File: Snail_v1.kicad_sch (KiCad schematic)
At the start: 29 parts, among them J1 PWM_Connector, J5 Conn_ARM_SWD_TagConnect_TC203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, U1 STM32G431K6Tx

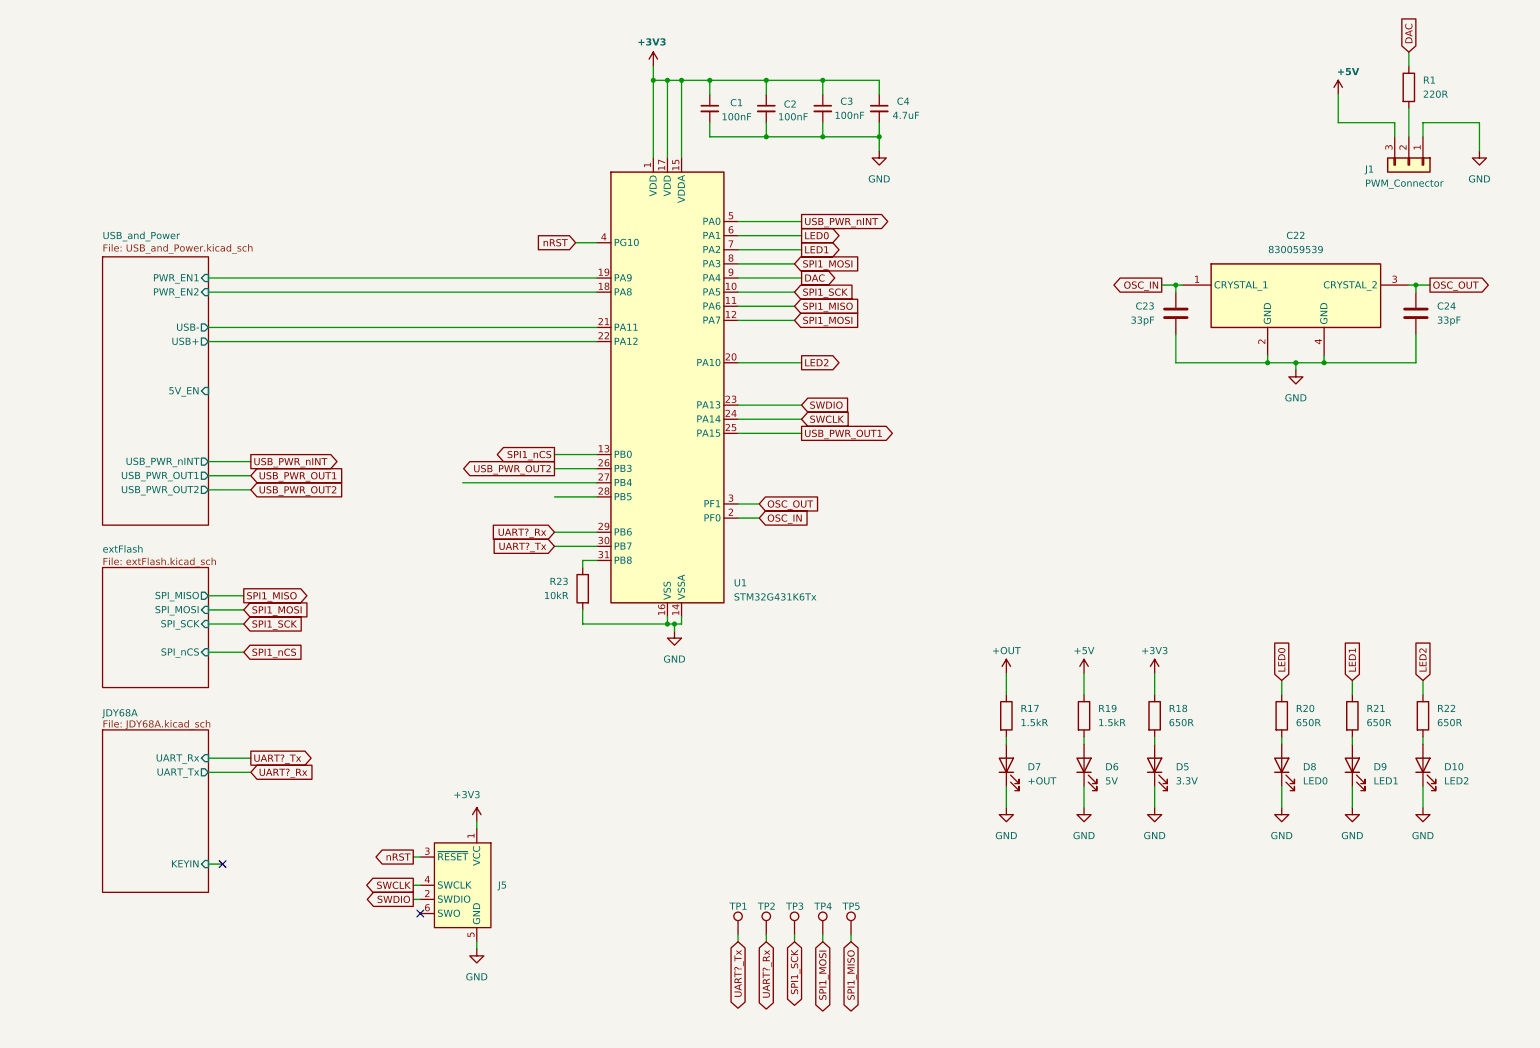
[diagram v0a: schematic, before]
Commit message: Did Silkscreen + added images of PCBA
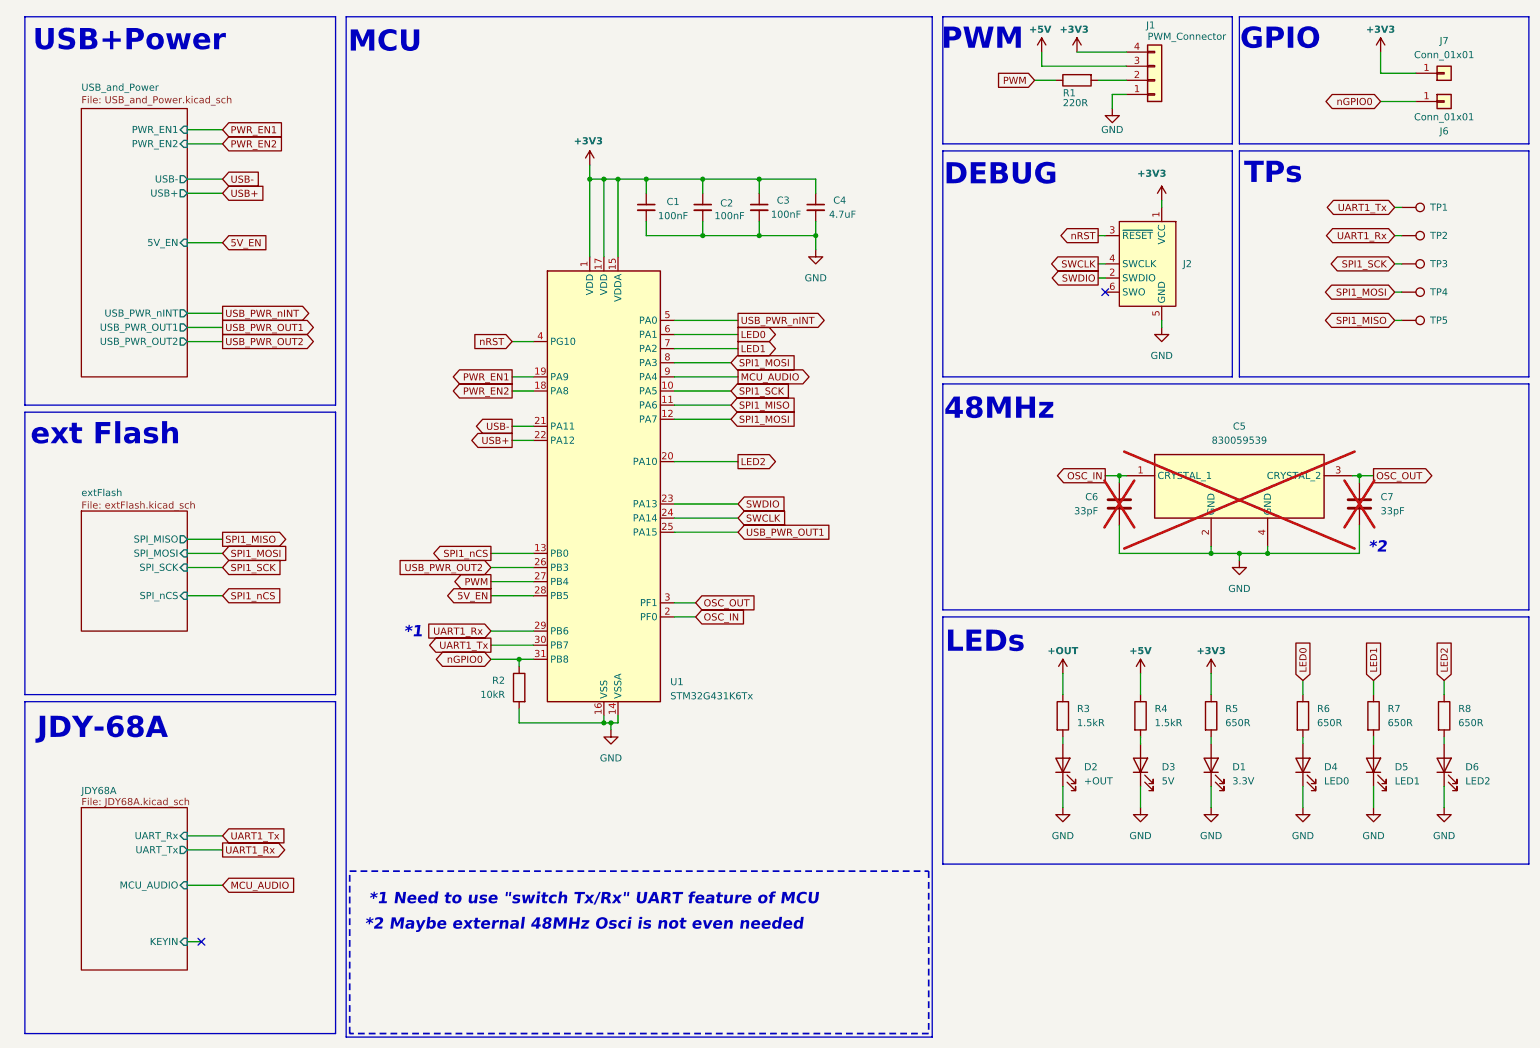
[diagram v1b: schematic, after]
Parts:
- removed J1: PWM_Connector, Connector_PinHeader_2.54mm:PinHeader_1x03_P2.54mm_Vertical, symbol Connector_Generic:Conn_01x03
- added J1: PWM_Connector, Connector_PinHeader_2.54mm:PinHeader_1x04_P2.54mm_Vertical, symbol Connector_Generic:Conn_01x04
- added J6, J7: Conn_01x01, Connector_Wire:SolderWirePad_1x01_SMD_1.5x3mm, symbol Connector_Generic:Conn_01x01
- C5: renamed from C22; now not fitted
- C6: renamed from C23; now not fitted
- C7: renamed from C24; now not fitted
- renumbered D5 to D1, D7 to D2, D6 to D3, D8 to D4, D9 to D5, D10 to D6, J5 to J2, R23 to R2, R17 to R3, R19 to R4, R18 to R5, R20 to R6, R21 to R7, R22 to R8
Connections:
- net +3V3: now also J1.4 (Pin_4), J7.1 (Pin_1)
- net +5V: now also J1.3 (Pin_3)
- net GND: now also J1.1 (Pin_1)
- net at R1.2: now also J1.2 (Pin_2)
- net PWM: now reaches U1.27 (PB4)
- net PWM: now also R1.1
- net 5V_EN: now reaches U1.28 (PB5)
- net nGPIO0: now reaches R2.1, U1.31 (PB8)
- net nGPIO0: now also J6.1 (Pin_1)
- net DAC renamed MCU_AUDIO
- net MCU_AUDIO: no longer R1.1
- net UART?_Rx renamed UART1_Rx
- net UART?_Tx renamed UART1_Tx
- net USB_and_Power/PWR_EN1 renamed PWR_EN1
- net USB_and_Power/PWR_EN2 renamed PWR_EN2
- net USB_and_Power/USB+ renamed USB+
- net USB_and_Power/USB- renamed USB-
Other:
- sheet JDY68A ports: added MCU_AUDIO; removed none
- note added: "*1"
- note added: "*1 Need to use "switch Tx/Rx" UART feature of MCU"
- note added: "*2"
- note added: "*2 Maybe external 48MHz Osci is not even needed"
- note added: "48MHz"
- note added: "DEBUG"
- note added: "GPIO"
- note added: "JDY-68A"
- note added: "LEDs"
- note added: "MCU"
- note added: "PWM"
- note added: "TPs"
- note added: "USB+Power"
- note added: "ext Flash"
- moved on the sheet: C1, C2, C3, C4, D1, D2, D3, D4, D5, D6, J2, R1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

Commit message: Added missing AMP_nSD connection to MCU via 5V_EN
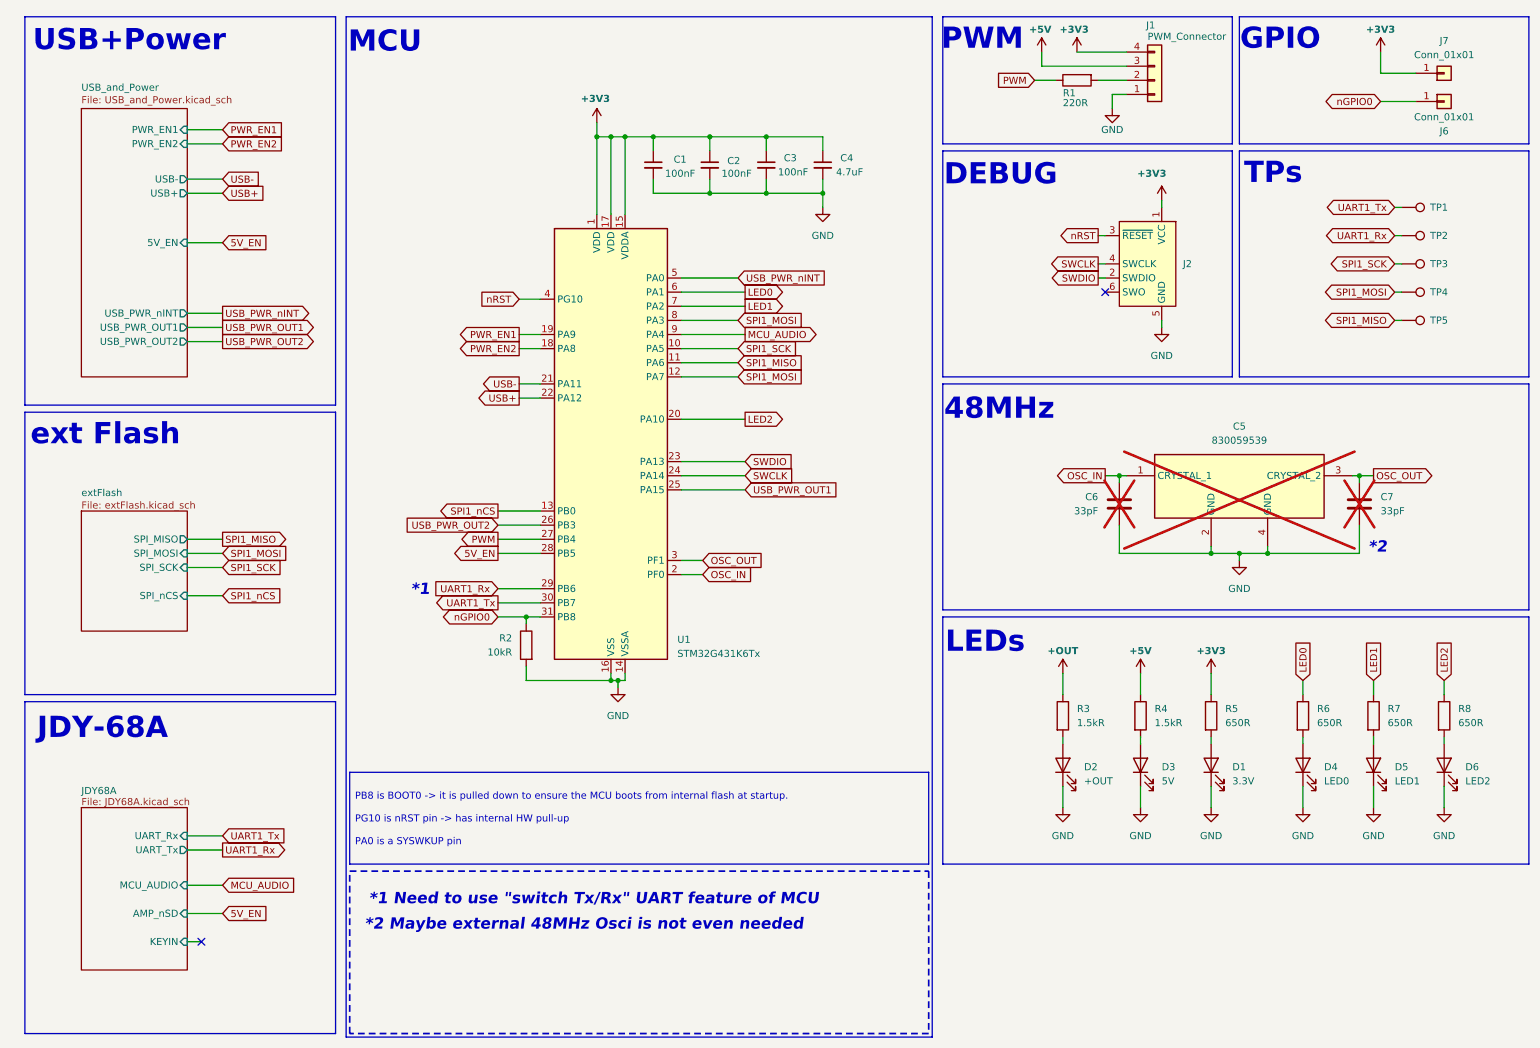
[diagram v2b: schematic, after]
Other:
- sheet JDY68A ports: added AMP_nSD; removed none
- moved on the sheet: C1, C2, C3, C4, R2, U1

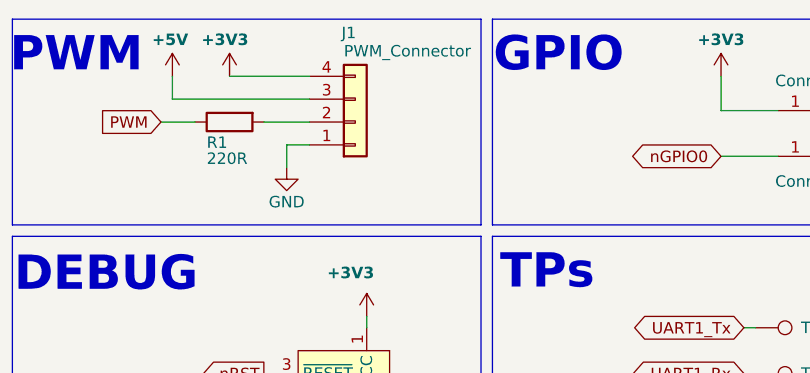
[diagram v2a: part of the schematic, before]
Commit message: Changed layout + added dimensions
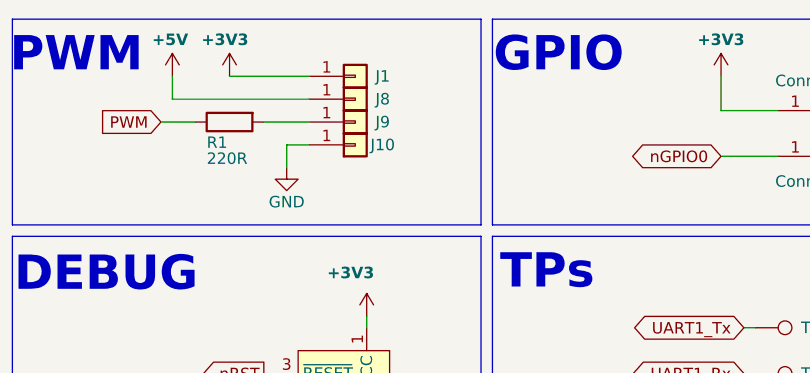
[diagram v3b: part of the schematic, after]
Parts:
- removed J1: PWM_Connector, Connector_PinHeader_2.54mm:PinHeader_1x04_P2.54mm_Vertical, symbol Connector_Generic:Conn_01x04
- added J1, J10, J8, J9: Conn_01x01, Connector_Wire:SolderWirePad_1x01_SMD_1.5x3mm, symbol Connector_Generic:Conn_01x01
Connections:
- net +3V3: now also J1.1 (Pin_1)
- net +5V: now also J8.1 (Pin_1)
- net GND: now also J10.1 (Pin_1)
- net at R1.2: now also J9.1 (Pin_1)
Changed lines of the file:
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@@
+	)
+	(symbol
+		(lib_id "Connector_Generic:Conn_01x01")
+		(at 215.9 26.67 0)
+		(mirror x)
+		(unit 1)
+		(exclude_from_sim no)
+		(in_bom yes)
+		(on_board yes)
+		(dnp no)
+		(property "Reference" "J10"
+			(at 218.948 26.67 0)
+			(effects
+				(font
+					(size 1.27 1.27)
+				)
+			)
+		)
+		(property "Value" "Conn_01x01"
+			(at 223.52 26.67 0)
+			(effects
+				(font
+					(size 1.27 1.27)
+				)
+				(hide yes)
+			)
+		)
+		(property "Footprint" "Connector_Wire:SolderWirePad_1x01_SMD_1.5x3mm"
+			(at 215.9 26.67 0)
+			(effects
+				(font
+					(size 1.27 1.27)
+				)
+				(hide yes)
+			)
+		)
+		(property "Datasheet" "~"
+			(at 215.9 26.67 0)
+			(effects
+				(font
+					(size 1.27 1.27)
+				)
+				(hide yes)
+			)
+		)
+		(property "Description" "Generic connector, single row, 01x01, script generated (kicad-library-utils/schlib/autogen/connector/)"
+			(at 215.9 26.67 0)
+			(effects
+				(font
+					(size 1.27 1.27)
+				)
+				(hide yes)
+			)
+		)
+		(pin "1"
+		)
+		(instances
+			(project "Snail_v1"
+				(path "/98695d9f-8521-4f7d-bb41-f22c1215a8e7"
+					(reference "J10")
+					(unit 1)
+				)
+			)
+		)
 	)
 	(symbol
@@
 	)
 	(symbol
+		(lib_id "Connector_Generic:Conn_01x01")
+		(at 215.9 24.13 0)
+		(mirror x)
+		(unit 1)
+		(exclude_from_sim no)
+		(in_bom yes)
+		(on_board yes)
+		(dnp no)
+		(property "Reference" "J9"
+			(at 218.948 24.13 0)
+			(effects
+				(font
+					(size 1.27 1.27)
+				)
+			)
+		)
+		(property "Value" "Conn_01x01"
+			(at 223.52 24.13 0)
+			(effects
+				(font
+					(size 1.27 1.27)
+				)
+				(hide yes)
+			)
+		)
+		(property "Footprint" "Connector_Wire:SolderWirePad_1x01_SMD_1.5x3mm"
+			(at 215.9 24.13 0)
+			(effects
+				(font
+					(size 1.27 1.27)
+				)
+				(hide yes)
+			)
+		)
+		(property "Datasheet" "~"
+			(at 215.9 24.13 0)
+			(effects
+				(font
+					(size 1.27 1.27)
+				)
+				(hide yes)
+			)
+		)
+		(property "Description" "Generic connector, single row, 01x01, script generated (kicad-library-utils/schlib/autogen/connector/)"
+			(at 215.9 24.13 0)
+			(effects
+				(font
+					(size 1.27 1.27)
+				)
+				(hide yes)
+			)
+		)
+		(pin "1"
+		)
+		(instances
+			(project "Snail_v1"
+				(path "/98695d9f-8521-4f7d-bb41-f22c1215a8e7"
+					(reference "J9")
+					(unit 1)
+				)
+			)
+		)
+	)
+	(symbol
 		(lib_id "Device:LED")
 		(at 255.27 147.32 90)
@@
 	)
 	(symbol
-		(lib_id "Connector_Generic:Conn_01x04")
-		(at 215.9 24.13 0)
-		(mirror x)
-		(unit 1)
-		(exclude_from_sim no)
-		(in_bom yes)
-		(on_board yes)
-		(dnp no)
-		(property "Reference" "J1"
-			(at 214.376 14.224 0)
-			(effects
-				(font
-					(size 1.27 1.27)
-				)
-				(justify left)
-			)
-		)
-		(property "Value" "PWM_Connector"
-			(at 214.63 16.256 0)
-			(effects
-				(font
-					(size 1.27 1.27)
-				)
-				(justify left)
-			)
-		)
-		(property "Footprint" "Connector_PinHeader_2.54mm:PinHeader_1x04_P2.54mm_Vertical"
-			(at 215.9 24.13 0)
-			(effects
-				(font
-					(size 1.27 1.27)
-				)
-				(hide yes)
-			)
-		)
-		(property "Datasheet" "~"
-			(at 215.9 24.13 0)
-			(effects
-				(font
-					(size 1.27 1.27)
-				)
-				(hide yes)
-			)
-		)
-		(property "Description" "Generic connector, single row, 01x04, script generated (kicad-library-utils/schlib/autogen/connector/)"
-			(at 215.9 24.13 0)
-			(effects
-				(font
-					(size 1.27 1.27)
-				)
-				(hide yes)
-			)
-		)
-		(pin "1"
-		)
-		(pin "3"
-		)
-		(pin "2"
-		)
-		(pin "4"
-		)
-		(instances
-			(project ""
-				(path "/98695d9f-8521-4f7d-bb41-f22c1215a8e7"
-					(reference "J1")
-					(unit 1)
-				)
-			)
-		)
-	)
-	(symbol
 		(lib_id "Connector:TestPoint")
 		(at 260.35 57.15 270)
@@
 				(path "/98695d9f-8521-4f7d-bb41-f22c1215a8e7"
 					(reference "#PWR049")
+					(unit 1)
+				)
+			)
+		)
+	)
+	(symbol
+		(lib_id "Connector_Generic:Conn_01x01")
+		(at 215.9 19.05 0)
+		(mirror x)
+		(unit 1)
+		(exclude_from_sim no)
+		(in_bom yes)
+		(on_board yes)
+		(dnp no)
+		(property "Reference" "J1"
+			(at 218.948 19.05 0)
+			(effects
+				(font
+					(size 1.27 1.27)
+				)
+			)
+		)
+		(property "Value" "Conn_01x01"
+			(at 223.52 19.05 0)
+			(effects
+				(font
+					(size 1.27 1.27)
+				)
+				(hide yes)
+			)
+		)
+		(property "Footprint" "Connector_Wire:SolderWirePad_1x01_SMD_1.5x3mm"
+			(at 215.9 19.05 0)
+			(effects
+				(font
+					(size 1.27 1.27)
+				)
+				(hide yes)
+			)
+		)
+		(property "Datasheet" "~"
+			(at 215.9 19.05 0)
+			(effects
+				(font
+					(size 1.27 1.27)
+				)
+				(hide yes)
+			)
+		)
+		(property "Description" "Generic connector, single row, 01x01, script generated (kicad-library-utils/schlib/autogen/connector/)"
+			(at 215.9 19.05 0)
+			(effects
+				(font
+					(size 1.27 1.27)
+				)
+				(hide yes)
+			)
+		)
+		(pin "1"
+		)
+		(instances
+			(project "Snail_v1"
+				(path "/98695d9f-8521-4f7d-bb41-f22c1215a8e7"
+					(reference "J1")
 					(unit 1)
 				)
@@
 					(unit 1)
 				)
+			)
+		)
+	)
+	(symbol
+		(lib_id "Connector_Generic:Conn_01x01")
+		(at 215.9 21.59 0)
+		(mirror x)
+		(unit 1)
+		(exclude_from_sim no)
+		(in_bom yes)
+		(on_board yes)
+		(dnp no)
+		(property "Reference" "J8"
+			(at 218.948 21.59 0)
+			(effects
+				(font
+					(size 1.27 1.27)
+				)
+			)
+		)
+		(property "Value" "Conn_01x01"
+			(at 223.52 21.59 0)
+			(effects
+				(font
+					(size 1.27 1.27)
+				)
+				(hide yes)
+			)
+		)
+		(property "Footprint" "Connector_Wire:SolderWirePad_1x01_SMD_1.5x3mm"
+			(at 215.9 21.59 0)
+			(effects
+				(font
+					(size 1.27 1.27)
+				)
+				(hide yes)
+			)
+		)
+		(property "Datasheet" "~"
+			(at 215.9 21.59 0)
+			(effects
+				(font
+					(size 1.27 1.27)
+				)
+				(hide yes)
+			)
+		)
+		(property "Description" "Generic connector, single row, 01x01, script generated (kicad-library-utils/schlib/autogen/connector/)"
+			(at 215.9 21.59 0)
+			(effects
+				(font
+					(size 1.27 1.27)
+				)
+				(hide yes)
+			)
+		)
+		(pin "1"
+		)
+		(instances
+			(project "Snail_v1"
+				(path "/98695d9f-8521-4f7d-bb41-f22c1215a8e7"
+					(reference "J8")
+					(unit 1)
+				)

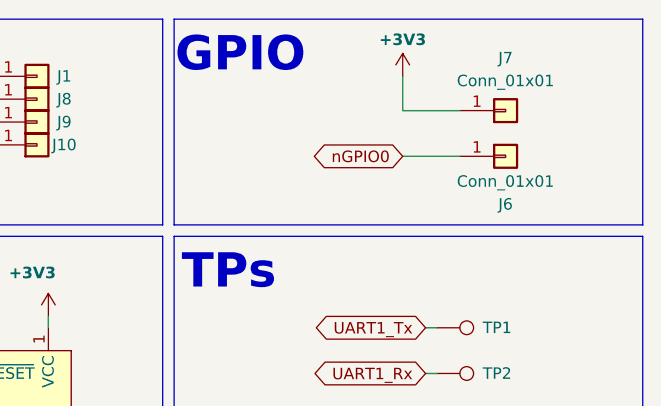
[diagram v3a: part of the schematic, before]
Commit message: Added +BAT and GND Pad to design
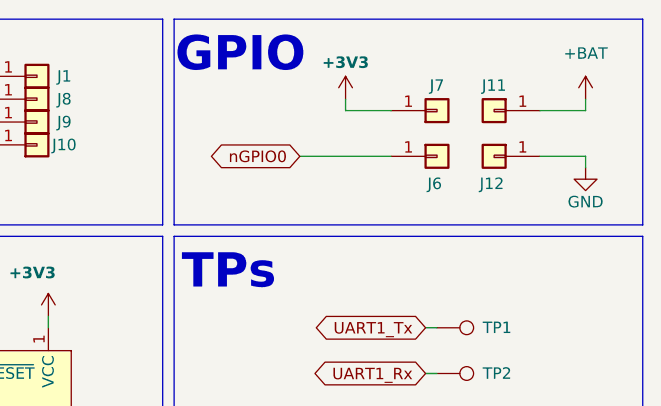
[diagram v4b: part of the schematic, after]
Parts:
- added J11, J12: Conn_01x01, Connector_Wire:SolderWirePad_1x01_SMD_1.5x3mm, symbol Connector_Generic:Conn_01x01
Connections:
- net GND: now also J12.1 (Pin_1)
- new net +BAT: J11.1 (Pin_1)
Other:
- moved on the sheet: J6, J7
